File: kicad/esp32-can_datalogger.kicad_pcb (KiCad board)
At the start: 2 copper layers, 100 x 60 mm, 60 parts, among them J1 USB_C_Receptacle_USB2.0_16P, J2 USB_C_Receptacle_USB2.0_16P, J3 USB_C_Receptacle_USB2.0_16P, J4 USB_C_Receptacle_USB2.0_16P, J5 Conn_01x04_Socket, J6 Conn_Coaxial, J7 MicroSD, J8 USB_C_Receptacle_USB2.0_16P, J9 USB_C_Receptacle_USB2.0_16P, SW1 SW_Push, SW2 SW_Push, SW3 SW_Push, SW4 SW_Push, U2 PA1616D, U3 PI4ULS3V204LEX, U4 AZ1117-1.8, U5 TJA1051T, U6 TJA1051T, U7 ICM-20948

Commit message: minor updates
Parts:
- renumbered J8 to J4, J9 to J5, J4 to J6, J6 to J7, J7 to J8, J5 to J9, JP4 to JP3
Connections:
- D3 pad 3: unconnected-(D3-VSS-Pad3) -> GND

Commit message: minor updates
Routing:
- net Net-(J5-CC1): track 4.26 -> 3.30 mm

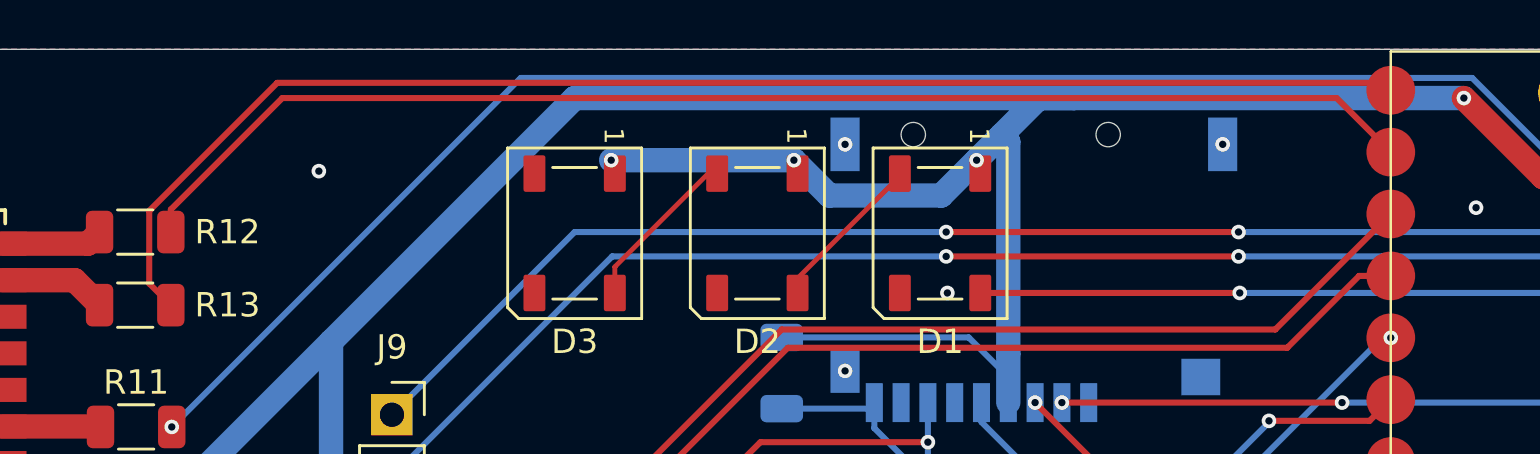
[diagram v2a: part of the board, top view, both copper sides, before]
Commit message: switch RX-TX for GPS
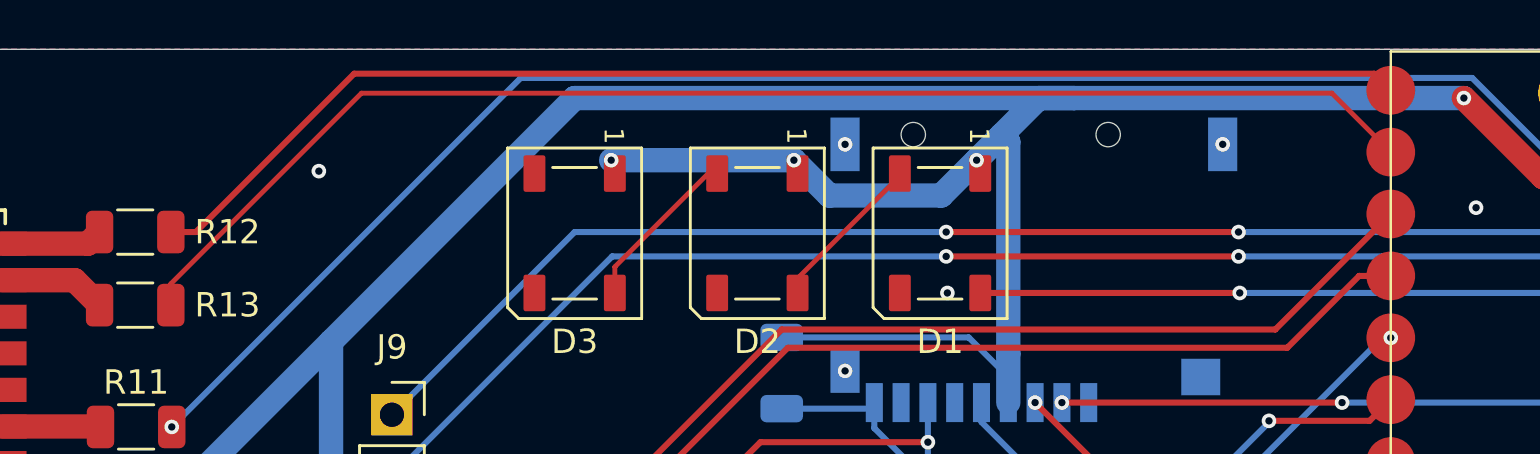
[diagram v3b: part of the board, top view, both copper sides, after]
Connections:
- U1 pad 1: GPS_TX -> GPS_RX
- U1 pad 2: GPS_RX -> GPS_TX
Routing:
- net GPS_TX: track 57.1 -> 55.2 mm
- net GPS_RX: track 53.8 -> 53.0 mm
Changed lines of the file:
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@@
 		(capping no)
 		(filling no)
-		(zone_defaults)
 		(pcbplotparams
 			(layerselection 0x00000000_00000000_55555555_5755f5ff)
@@
 			(size 2 2)
 			(layers "F.Cu" "F.Mask" "F.Paste")
-			(net "GPS_TX")
+			(net "GPS_RX")
 			(pinfunction "TX_1")
 			(pintype "output")
@@
 			(size 2 2)
 			(layers "F.Cu" "F.Mask" "F.Paste")
-			(net "GPS_RX")
+			(net "GPS_TX")
 			(pinfunction "RX_2")
 			(pintype "input")
@@
 	)
 	(segment
-		(start 75.0375 76.6299)
-		(end 80.2924 71.375)
-		(width 0.25)
+		(start 75.925 79.625)
+		(end 83.75 71.8)
+		(width 0.2)
 		(layer "F.Cu")
 		(net "GPS_TX")
 	)
 	(segment
-		(start 80.2924 71.375)
-		(end 125.695 71.375)
-		(width 0.25)
+		(start 75.925 80.5)
+		(end 75.925 79.625)
+		(width 0.2)
 		(layer "F.Cu")
 		(net "GPS_TX")
 	)
 	(segment
-		(start 75.925 80.5)
-		(end 75.0375 79.6125)
-		(width 0.25)
+		(start 123.58 71.8)
+		(end 126 74.22)
+		(width 0.2)
 		(layer "F.Cu")
 		(net "GPS_TX")
 	)
 	(segment
-		(start 75.0375 79.6125)
-		(end 75.0375 76.6299)
-		(width 0.25)
+		(start 83.75 71.8)
+		(end 123.58 71.8)
+		(width 0.2)
 		(layer "F.Cu")
 		(net "GPS_TX")
 	)
 	(segment
-		(start 123.78 72)
-		(end 126 74.22)
+		(start 76.95 77.5)
+		(end 83.45 71)
 		(width 0.25)
 		(layer "F.Cu")
@@
 	)
 	(segment
-		(start 75.925 77.5)
-		(end 75.925 76.575)
+		(start 83.45 71)
+		(end 125.32 71)
 		(width 0.25)
 		(layer "F.Cu")
@@
 	)
 	(segment
-		(start 75.925 76.575)
-		(end 80.5 72)
+		(start 125.32 71)
+		(end 126 71.68)
 		(width 0.25)
 		(layer "F.Cu")
@@
 	)
 	(segment
-		(start 80.5 72)
-		(end 123.78 72)
+		(start 75.925 77.5)
+		(end 76.95 77.5)
 		(width 0.25)
 		(layer "F.Cu")
